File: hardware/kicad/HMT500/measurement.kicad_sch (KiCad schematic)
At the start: 15 parts, among them J3 SM04B-SRSS-TB, U5 PCAP04-AQFM-24, U6 ADS1220IPWR

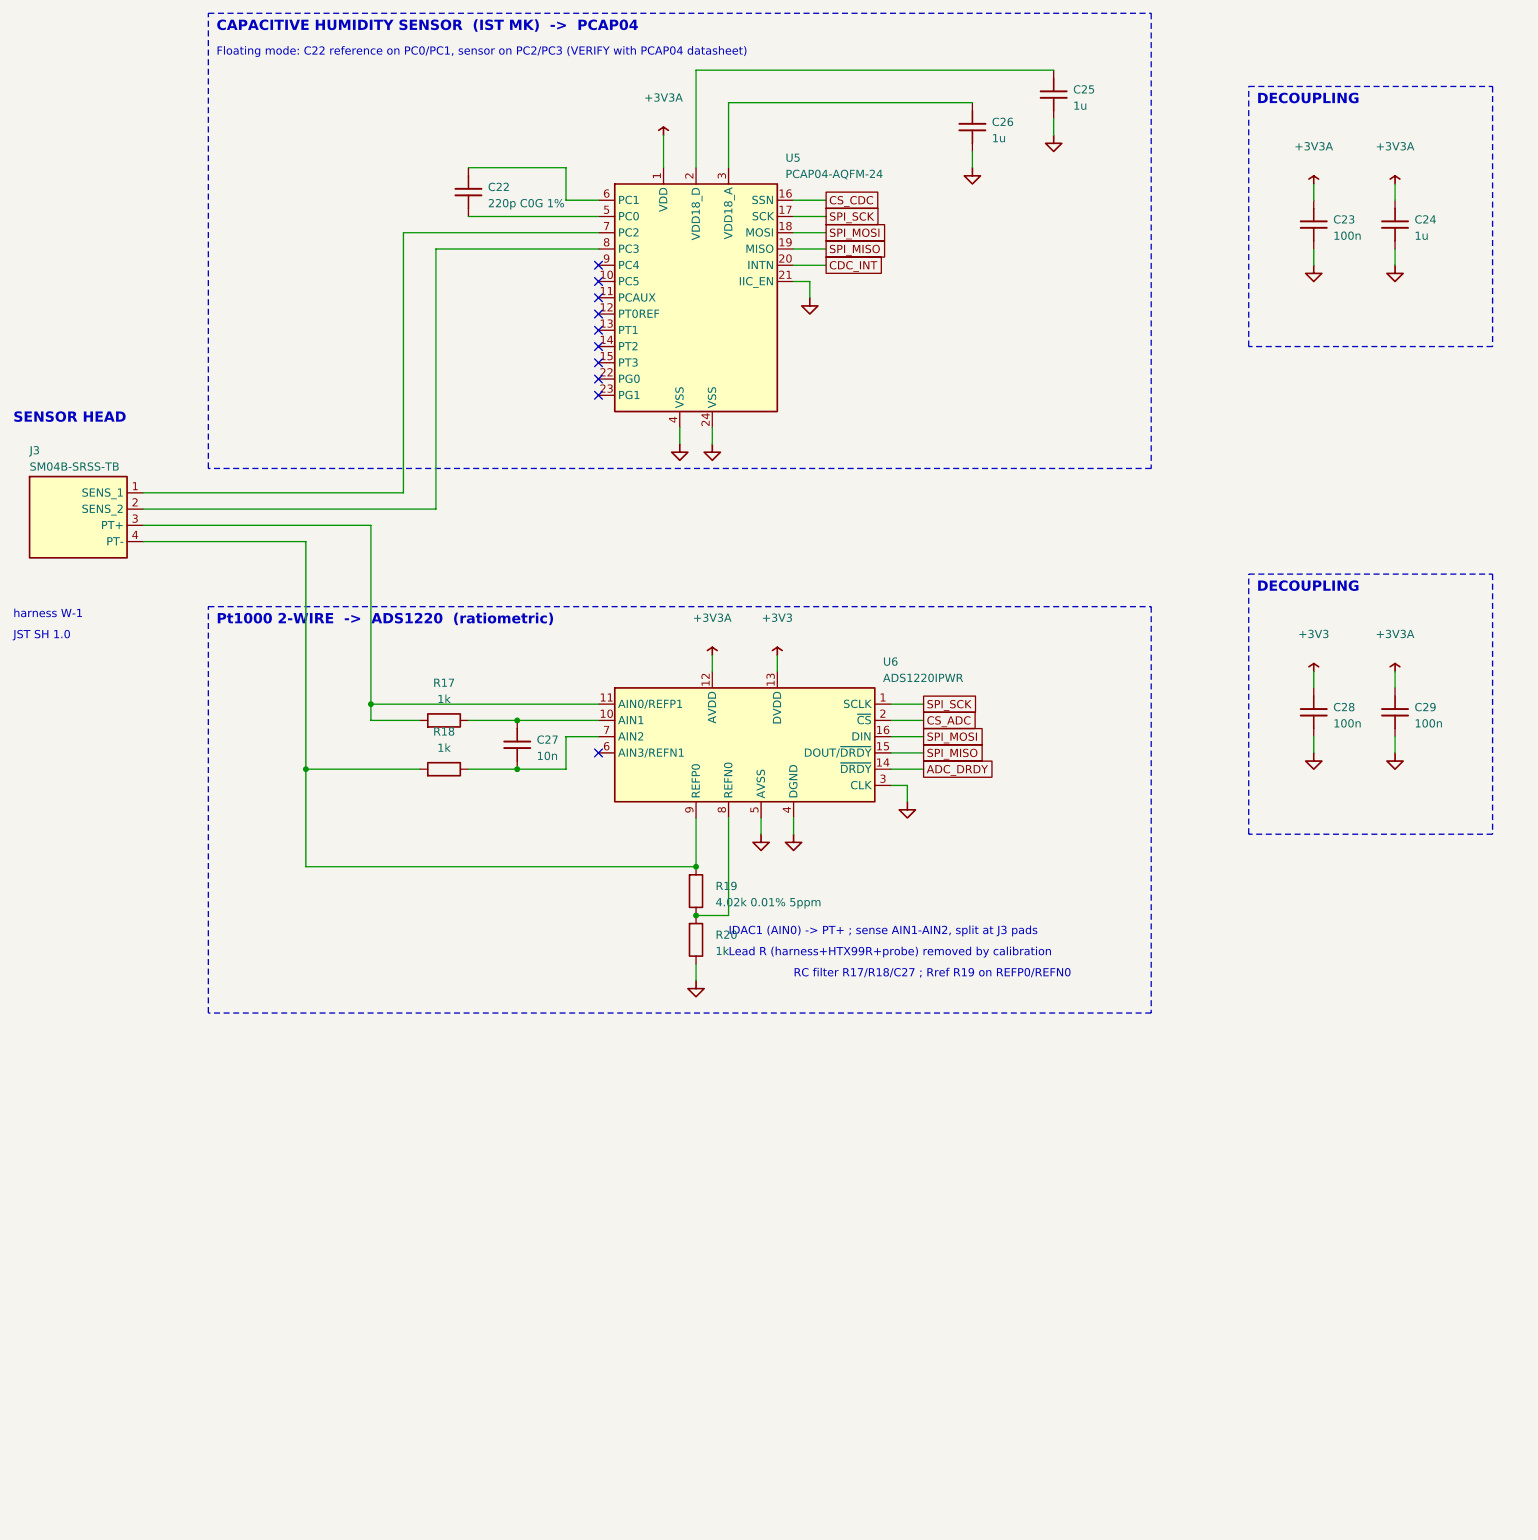
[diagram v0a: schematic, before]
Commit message: Schematic drawing rules: no overlapping text, Korean font, distinct net names
- Generator places reference/value text automatically, clear of symbol bodies,
  pins, wires, labels, notes and box edges; validation fails on any overlap
  (also note text vs wires/power names and bodies vs box edges)
- Fix 180-degree parts (LED) whose justification KiCad mirrors
- Styles: reference bold, value normal, power nets italic, signal nets boxed labels
- Korean box subtitles and legend in NanumGothic TrueType (stroke font has no Hangul)
- Nets renamed where they matched part or pin names: LED -> STAT_LED, EF_ILIM/IMON/DVDT
- J1 GH mounting pads removed from the symbol (PCB only); connector sheet re-spaced
- Schematic PDF export added; tests for net naming and Hangul font

Co-Authored-By: Claude Opus 5.5 <noreply@anthropic.com>
Claude-Session: https://claude.ai/code/session_01JA2o8uJsqp9Vzsg4b665ev
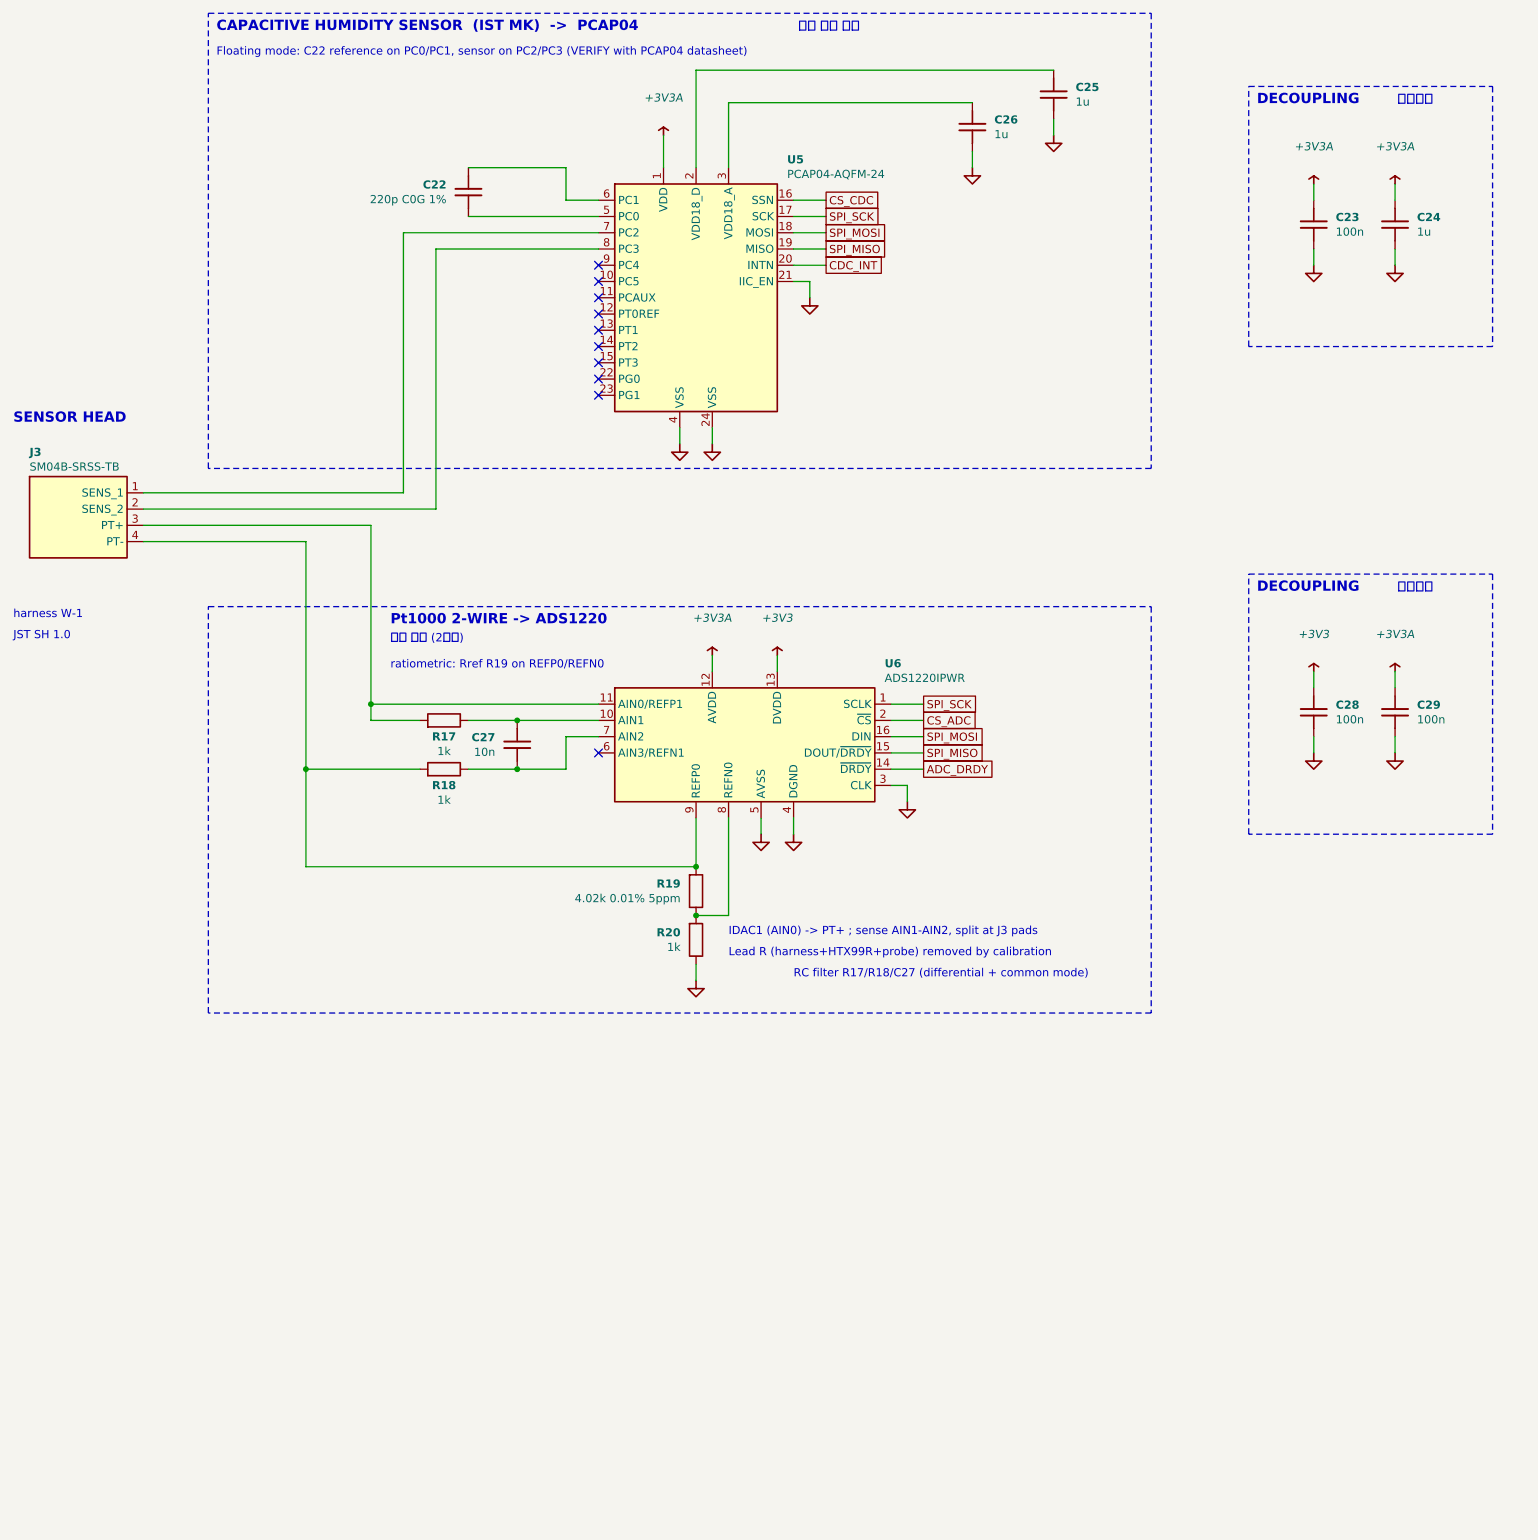
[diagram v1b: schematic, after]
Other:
- note added: "Pt1000 2-WIRE -> ADS1220"
- note added: "RC filter R17/R18/C27 (differential + common mode)"
- note added: "ratiometric: Rref R19 on REFP0/REFN0"
- note added: "바이패스"
- note added: "습도 센서 측정"
- note added: "온도 측정 (2선식)"
- note removed: "Pt1000 2-WIRE -> ADS1220 (ratiometric)"
- note removed: "RC filter R17/R18/C27 ; Rref R19 on REFP0/REFN0"

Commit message: Schematic v0.6: parts cleanup (91 -> 75) and PCB temperature sensing
- Removed: fault pull-ups R11-R15 (MCU internal pull-ups), status LED D3/R16
  (not visible after potting), RS-485 R60/R61/D60/D61 (THVD2450 built-in
  protection), VREF+ filter FB2/C19 (MCU ADC only for diagnostics), C11/C2/C6
  (duplicated by adjacent capacitors); VREF+ tied to +3V3 with C20
- PCB temperature with no added parts: ADS1220 internal sensor at the measurement
  front, STM32G0 internal sensor mid-board; compensation plan in circuit-design 5B
- 63 nets, netlist check 0 errors; parts list regenerated; decision log #22/#23

Co-Authored-By: Claude Opus 5.5 <noreply@anthropic.com>
Claude-Session: https://claude.ai/code/session_01JA2o8uJsqp9Vzsg4b665ev
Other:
- note added: "PCB temp: ADS1220 internal sensor (TS mode)"
